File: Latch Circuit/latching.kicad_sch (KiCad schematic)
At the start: 9 parts

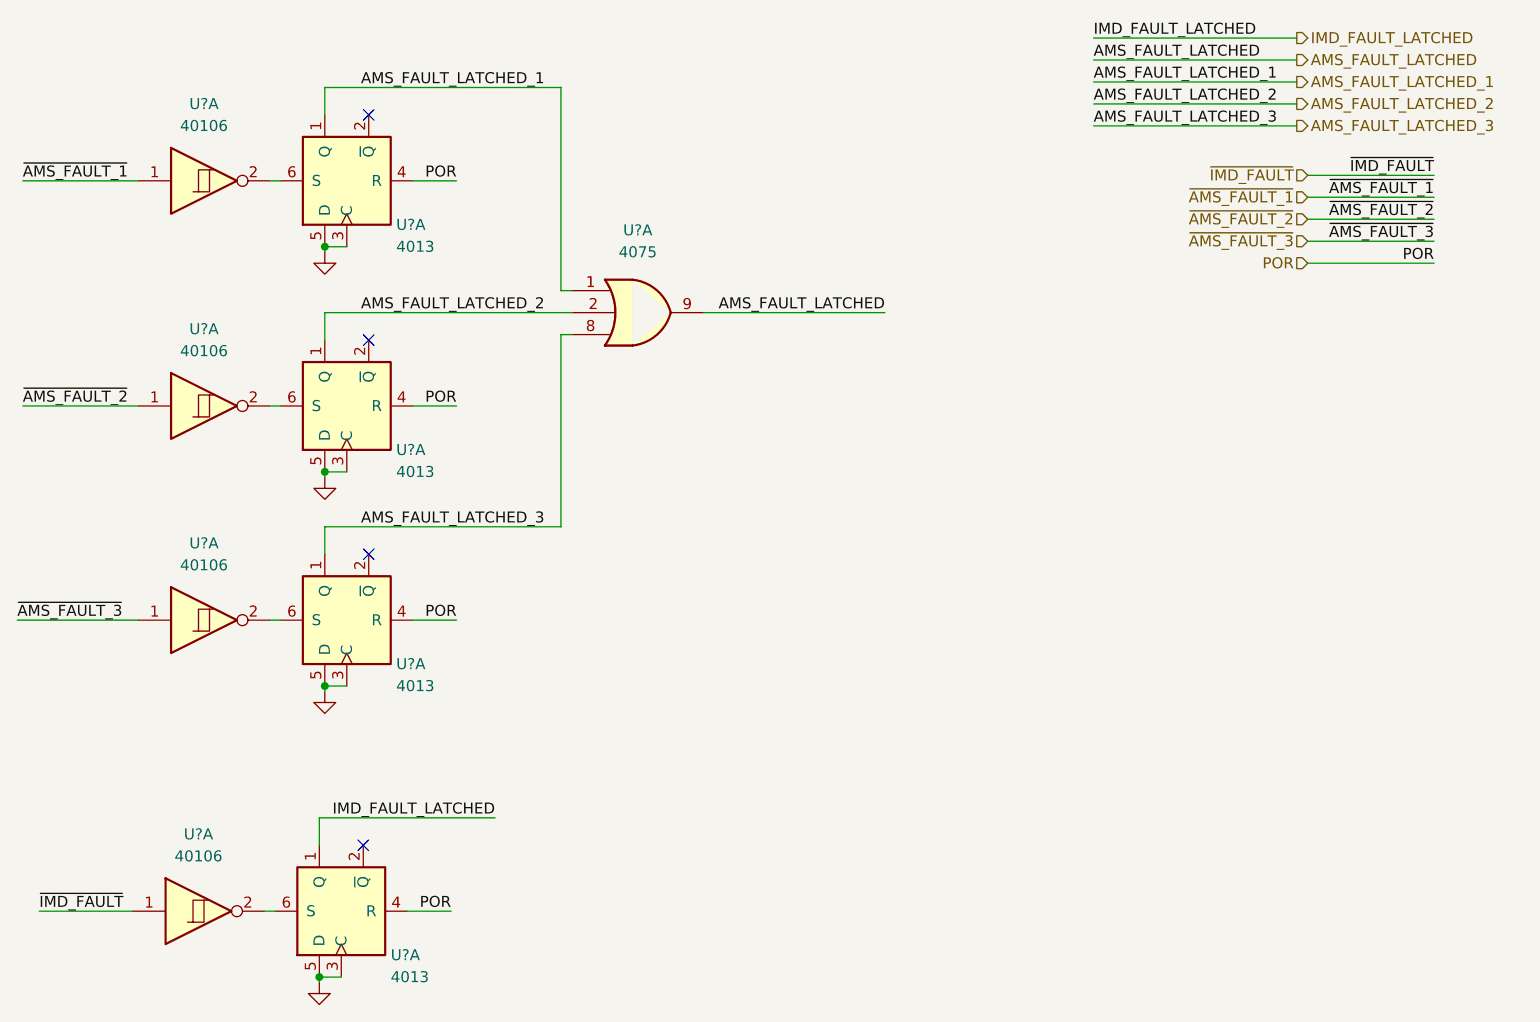
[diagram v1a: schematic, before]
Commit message: update schematic (ESF v1 submission)
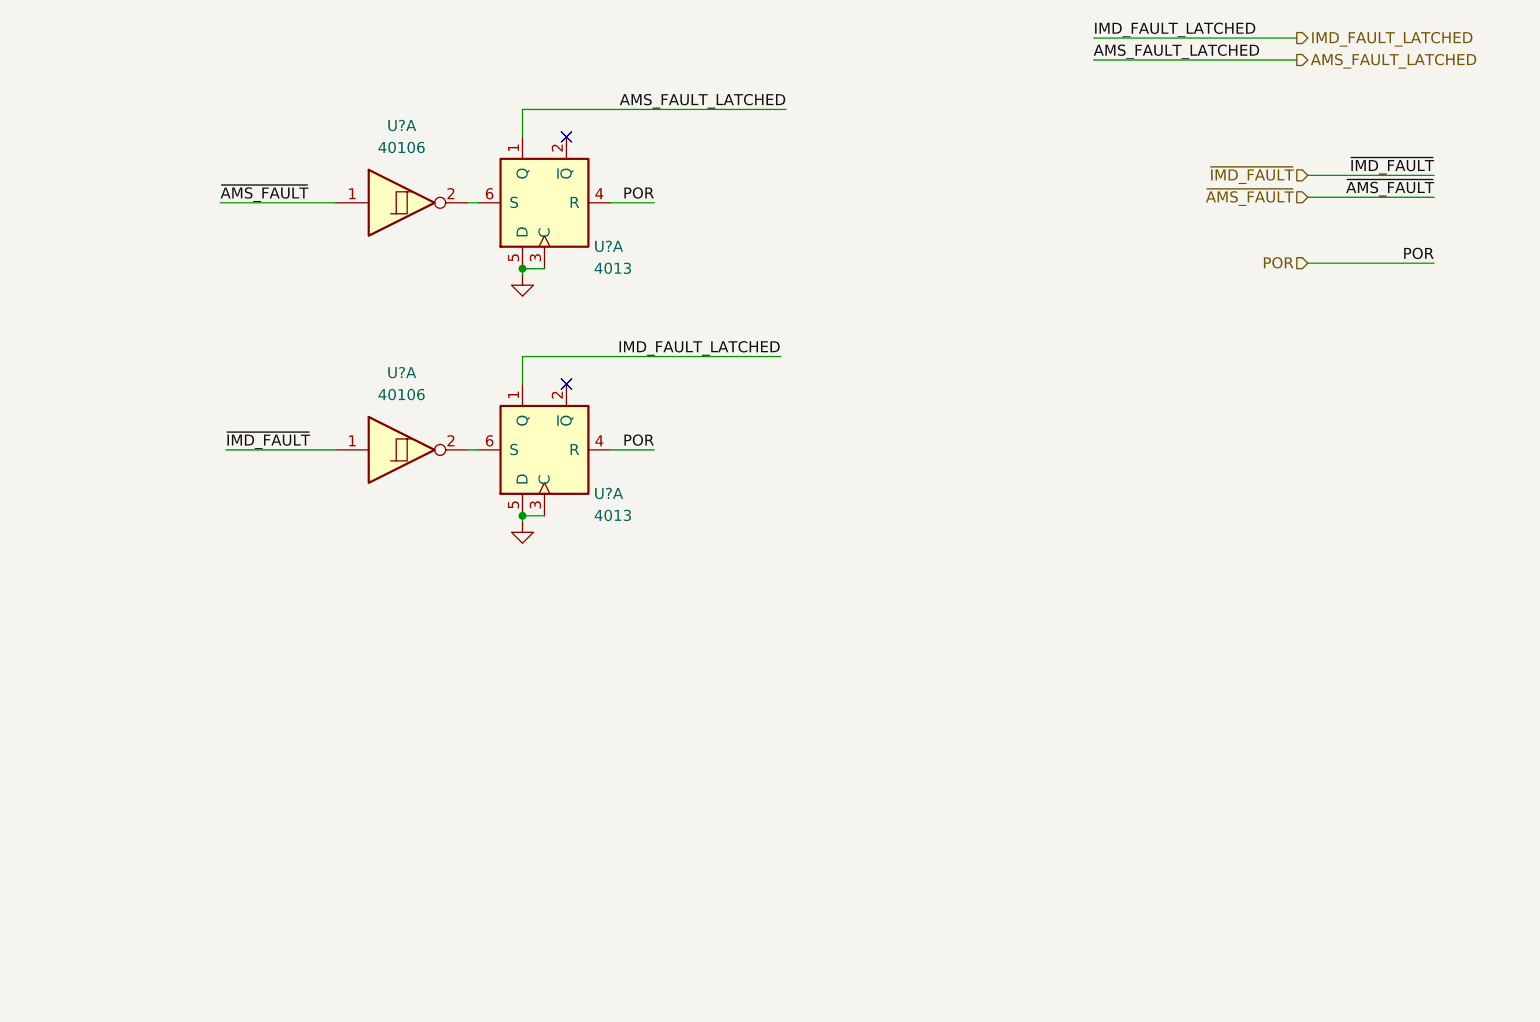
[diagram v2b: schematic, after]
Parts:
- removed U? (x2): 40106, symbol 4xxx:40106
- removed U? (x2): 4013, symbol 4xxx:4013
- removed U?: 4075, symbol 4xxx:4075
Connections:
- net AMS_FAULT_LATCHED_1 is gone; now on net AMS_FAULT_LATCHED: U?.1 (Q)
- net ~{AMS_FAULT_1} renamed ~{AMS_FAULT}
- no-connect marks 4 -> 2
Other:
- moved on the sheet: U?A
